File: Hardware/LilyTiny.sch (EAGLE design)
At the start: 14 parts, among them U1 ATTINY85

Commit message: Updating files to more clearly differentiate between Tiny/Twinkle
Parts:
- added LOGO2: SFE_LOGO_FLAME.1_INCH, SparkFun-Aesthetics:SFE_LOGO_FLAME.1_INCH
- added U$1: REVISION, SparkFun-Aesthetics:REVISION
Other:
- note added: "P.Lewis, T.Klopfenstein"
- note added: "V12"
- note removed: "Revised by: Pete Lewis"
- note removed: "V11"
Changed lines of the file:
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@@
 <?xml version="1.0" encoding="utf-8"?>
 <!DOCTYPE eagle SYSTEM "eagle.dtd">
-<eagle version="6.4">
+<eagle version="6.5.0">
 <drawing>
 <settings>
@@
 <grid distance="0.1" unitdist="inch" unit="inch" style="lines" multiple="1" display="no" altdistance="0.01" altunitdist="inch" altunit="inch"/>
 <layers>
-<layer number="1" name="Top" color="4" fill="1" visible="yes" active="no"/>
-<layer number="2" name="Route2" color="1" fill="3" visible="yes" active="no"/>
-<layer number="3" name="Route3" color="4" fill="3" visible="yes" active="no"/>
-<layer number="4" name="Route4" color="1" fill="4" visible="yes" active="no"/>
-<layer number="5" name="Route5" color="4" fill="4" visible="yes" active="no"/>
-<layer number="6" name="Route6" color="1" fill="8" visible="yes" active="no"/>
-<layer number="7" name="Route7" color="4" fill="8" visible="yes" active="no"/>
-<layer number="8" name="Route8" color="1" fill="2" visible="yes" active="no"/>
-<layer number="9" name="Route9" color="4" fill="2" visible="yes" active="no"/>
-<layer number="10" name="Route10" color="1" fill="7" visible="yes" active="no"/>
-<layer number="11" name="Route11" color="4" fill="7" visible="yes" active="no"/>
-<layer number="12" name="Route12" color="1" fill="5" visible="yes" active="no"/>
-<layer number="13" name="Route13" color="4" fill="5" visible="yes" active="no"/>
-<layer number="14" name="Route14" color="1" fill="6" visible="yes" active="no"/>
-<layer number="15" name="Route15" color="4" fill="6" visible="yes" active="no"/>
-<layer number="16" name="Bottom" color="1" fill="1" visible="yes" active="no"/>
-<layer number="17" name="Pads" color="2" fill="1" visible="yes" active="no"/>
-<layer number="18" name="Vias" color="2" fill="1" visible="yes" active="no"/>
-<layer number="19" name="Unrouted" color="6" fill="1" visible="yes" active="no"/>
-<layer number="20" name="Dimension" color="6" fill="1" visible="yes" active="no"/>
-<layer number="21" name="tPlace" color="16" fill="1" visible="yes" active="no"/>
-<layer number="22" name="bPlace" color="14" fill="1" visible="yes" active="no"/>
-<layer number="23" name="tOrigins" color="15" fill="1" visible="yes" active="no"/>
-<layer number="24" name="bOrigins" color="15" fill="1" visible="yes" active="no"/>
-<layer number="25" name="tNames" color="7" fill="1" visible="yes" active="no"/>
-<layer number="26" name="bNames" color="7" fill="1" visible="yes" active="no"/>
-<layer number="27" name="tValues" color="7" fill="1" visible="yes" active="no"/>
-<layer number="28" name="bValues" color="7" fill="1" visible="yes" active="no"/>
+<layer number="1" name="Top" color="4" fill="1" visible="no" active="no"/>
+<layer number="2" name="Route2" color="1" fill="3" visible="no" active="no"/>
+<layer number="3" name="Route3" color="4" fill="3" visible="no" active="no"/>
+<layer number="4" name="Route4" color="1" fill="4" visible="no" active="no"/>
+<layer number="5" name="Route5" color="4" fill="4" visible="no" active="no"/>
+<layer number="6" name="Route6" color="1" fill="8" visible="no" active="no"/>
+<layer number="7" name="Route7" color="4" fill="8" visible="no" active="no"/>
+<layer number="8" name="Route8" color="1" fill="2" visible="no" active="no"/>
+<layer number="9" name="Route9" color="4" fill="2" visible="no" active="no"/>
+<layer number="10" name="Route10" color="1" fill="7" visible="no" active="no"/>
+<layer number="11" name="Route11" color="4" fill="7" visible="no" active="no"/>
+<layer number="12" name="Route12" color="1" fill="5" visible="no" active="no"/>
+<layer number="13" name="Route13" color="4" fill="5" visible="no" active="no"/>
+<layer number="14" name="Route14" color="1" fill="6" visible="no" active="no"/>
+<layer number="15" name="Route15" color="4" fill="6" visible="no" active="no"/>
+<layer number="16" name="Bottom" color="1" fill="1" visible="no" active="no"/>
+<layer number="17" name="Pads" color="2" fill="1" visible="no" active="no"/>
+<layer number="18" name="Vias" color="2" fill="1" visible="no" active="no"/>
+<layer number="19" name="Unrouted" color="6" fill="1" visible="no" active="no"/>
+<layer number="20" name="Dimension" color="6" fill="1" visible="no" active="no"/>
+<layer number="21" name="tPlace" color="16" fill="1" visible="no" active="no"/>
+<layer number="22" name="bPlace" color="14" fill="1" visible="no" active="no"/>
+<layer number="23" name="tOrigins" color="15" fill="1" visible="no" active="no"/>
+<layer number="24" name="bOrigins" color="15" fill="1" visible="no" active="no"/>
+<layer number="25" name="tNames" color="7" fill="1" visible="no" active="no"/>
+<layer number="26" name="bNames" color="7" fill="1" visible="no" active="no"/>
+<layer number="27" name="tValues" color="7" fill="1" visible="no" active="no"/>
+<layer number="28" name="bValues" color="7" fill="1" visible="no" active="no"/>
 <layer number="29" name="tStop" color="7" fill="3" visible="no" active="no"/>
 <layer number="30" name="bStop" color="7" fill="6" visible="no" active="no"/>
@@
 <layer number="35" name="tGlue" color="7" fill="4" visible="no" active="no"/>
 <layer number="36" name="bGlue" color="7" fill="5" visible="no" active="no"/>
-<layer number="37" name="tTest" color="7" fill="1" visible="yes" active="no"/>
-<layer number="38" name="bTest" color="7" fill="1" visible="yes" active="no"/>
+<layer number="37" name="tTest" color="7" fill="1" visible="no" active="no"/>
+<layer number="38" name="bTest" color="7" fill="1" visible="no" active="no"/>
 <layer number="39" name="tKeepout" color="4" fill="11" visible="no" active="no"/>
 <layer number="40" name="bKeepout" color="1" fill="11" visible="no" active="no"/>
@@
 <layer number="44" name="Drills" color="7" fill="1" visible="no" active="no"/>
 <layer number="45" name="Holes" color="7" fill="1" visible="no" active="no"/>
-<layer number="46" name="Milling" color="3" fill="1" visible="yes" active="no"/>
-<layer number="47" name="Measures" color="7" fill="1" visible="yes" active="no"/>
-<layer number="48" name="Document" color="7" fill="1" visible="yes" active="no"/>
-<layer number="49" name="Reference" color="7" fill="1" visible="yes" active="no"/>
-<layer number="50" name="dxf" color="7" fill="1" visible="yes" active="no"/>
-<layer number="51" name="tDocu" color="6" fill="1" visible="yes" active="no"/>
-<layer number="52" name="bDocu" color="7" fill="1" visible="yes" active="no"/>
-<layer number="53" name="tGND_GNDA" color="7" fill="9" visible="yes" active="no"/>
-<layer number="54" name="bGND_GNDA" color="1" fill="9" visible="yes" active="no"/>
-<layer number="56" name="wert" color="7" fill="1" visible="yes" active="no"/>
+<layer number="46" name="Milling" color="3" fill="1" visible="no" active="no"/>
+<layer number="47" name="Measures" color="7" fill="1" visible="no" active="no"/>
+<layer number="48" name="Document" color="7" fill="1" visible="no" active="no"/>
+<layer number="49" name="Reference" color="7" fill="1" visible="no" active="no"/>
+<layer number="50" name="dxf" color="7" fill="1" visible="no" active="no"/>
+<layer number="51" name="tDocu" color="6" fill="1" visible="no" active="no"/>
+<layer number="52" name="bDocu" color="7" fill="1" visible="no" active="no"/>
+<layer number="53" name="tGND_GNDA" color="7" fill="9" visible="no" active="no"/>
+<layer number="54" name="bGND_GNDA" color="1" fill="9" visible="no" active="no"/>
+<layer number="56" name="wert" color="7" fill="1" visible="no" active="no"/>
 <layer number="91" name="Nets" color="2" fill="1" visible="yes" active="yes"/>
 <layer number="92" name="Busses" color="1" fill="1" visible="yes" active="yes"/>
@@
 <part name="FRAME2" library="SparkFun-Aesthetics" deviceset="FRAME-LETTER" device=""/>
 <part name="LOGO1" library="SparkFun-Aesthetics" deviceset="OSHW-LOGO" device="S"/>
+<part name="U$1" library="SparkFun-Aesthetics" deviceset="REVISION" device=""/>
+<part name="LOGO2" library="SparkFun-Aesthetics" deviceset="SFE_LOGO_FLAME" device=".1_INCH"/>
 </parts>
 <sheets>
@@
 <text x="32.766" y="1.27" size="2.1844" layer="91">2</text>
 <text x="32.766" y="-1.27" size="2.1844" layer="91">3</text>
-<text x="66.294" y="-82.296" size="1.778" layer="94">Revised by: Pete Lewis</text>
-<text x="119.38" y="-86.36" size="1.778" layer="94">V11</text>
+<text x="58.674" y="-87.376" size="1.778" layer="94">P.Lewis, T.Klopfenstein</text>
+<text x="119.38" y="-86.36" size="1.778" layer="94">V12</text>
 </plain>
 <instances>
@@
 <instance part="U$7" gate="G$1" x="30.48" y="7.62"/>
 <instance part="P+2" gate="1" x="0" y="-20.32"/>
-<instance part="U$8" gate="G$1" x="111.76" y="-66.04"/>
+<instance part="U$8" gate="G$1" x="116.84" y="-76.2"/>
 <instance part="JP1" gate="G$1" x="127" y="-63.5"/>
 <instance part="JP2" gate="G$1" x="127" y="-68.58"/>
@@
 <instance part="FRAME2" gate="G$2" x="27.94" y="-93.98"/>
 <instance part="LOGO1" gate="G$1" x="116.84" y="-48.26"/>
+<instance part="U$1" gate="G$1" x="29.718" y="-87.122"/>
+<instance part="LOGO2" gate="G$1" x="96.52" y="-58.42"/>
 </instances>
 <busses>

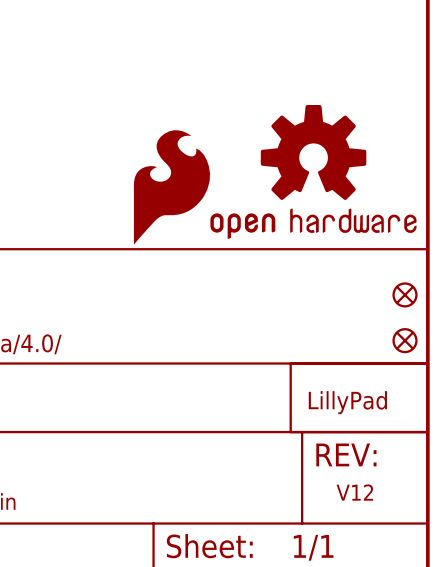
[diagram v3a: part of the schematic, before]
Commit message: Added regular fid to board. Deleted old gerbs
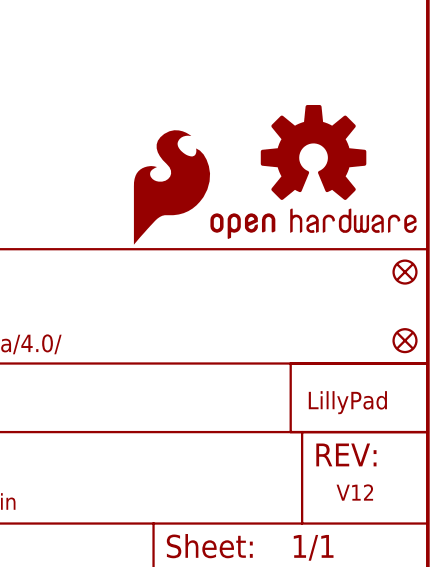
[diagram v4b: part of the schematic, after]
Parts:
- removed JP1, JP2: FIDUCIALUFIDUCIAL, SparkFun:FIDUCIALUFIDUCIAL
- added FID1, FID2: FIDUCIAL1X2, SparkFun-Aesthetics:FIDUCIAL1X2
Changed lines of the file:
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@@
 <part name="P+2" library="SparkFun" deviceset="VCC" device=""/>
 <part name="U$8" library="LilyPad-Wearables" deviceset="LOGO-LP" device="L"/>
-<part name="JP1" library="SparkFun" deviceset="FIDUCIAL" device="UFIDUCIAL"/>
-<part name="JP2" library="SparkFun" deviceset="FIDUCIAL" device="UFIDUCIAL"/>
 <part name="FRAME2" library="SparkFun-Aesthetics" deviceset="FRAME-LETTER" device=""/>
 <part name="LOGO1" library="SparkFun-Aesthetics" deviceset="OSHW-LOGO" device="S"/>
 <part name="U$1" library="SparkFun-Aesthetics" deviceset="REVISION" device=""/>
 <part name="LOGO2" library="SparkFun-Aesthetics" deviceset="SFE_LOGO_FLAME" device=".1_INCH"/>
+<part name="FID1" library="SparkFun-Aesthetics" deviceset="FIDUCIAL" device="1X2"/>
+<part name="FID2" library="SparkFun-Aesthetics" deviceset="FIDUCIAL" device="1X2"/>
 </parts>
 <sheets>
@@
 <instance part="P+2" gate="1" x="0" y="-20.32"/>
 <instance part="U$8" gate="G$1" x="116.84" y="-76.2"/>
-<instance part="JP1" gate="G$1" x="127" y="-63.5"/>
-<instance part="JP2" gate="G$1" x="127" y="-68.58"/>
 <instance part="FRAME2" gate="G$1" x="-119.38" y="-93.98"/>
 <instance part="FRAME2" gate="G$2" x="27.94" y="-93.98"/>
@@
 <instance part="U$1" gate="G$1" x="29.718" y="-87.122"/>
 <instance part="LOGO2" gate="G$1" x="96.52" y="-58.42"/>
+<instance part="FID1" gate="G$1" x="127" y="-60.96"/>
+<instance part="FID2" gate="G$1" x="127" y="-68.58"/>
 </instances>
 <busses>

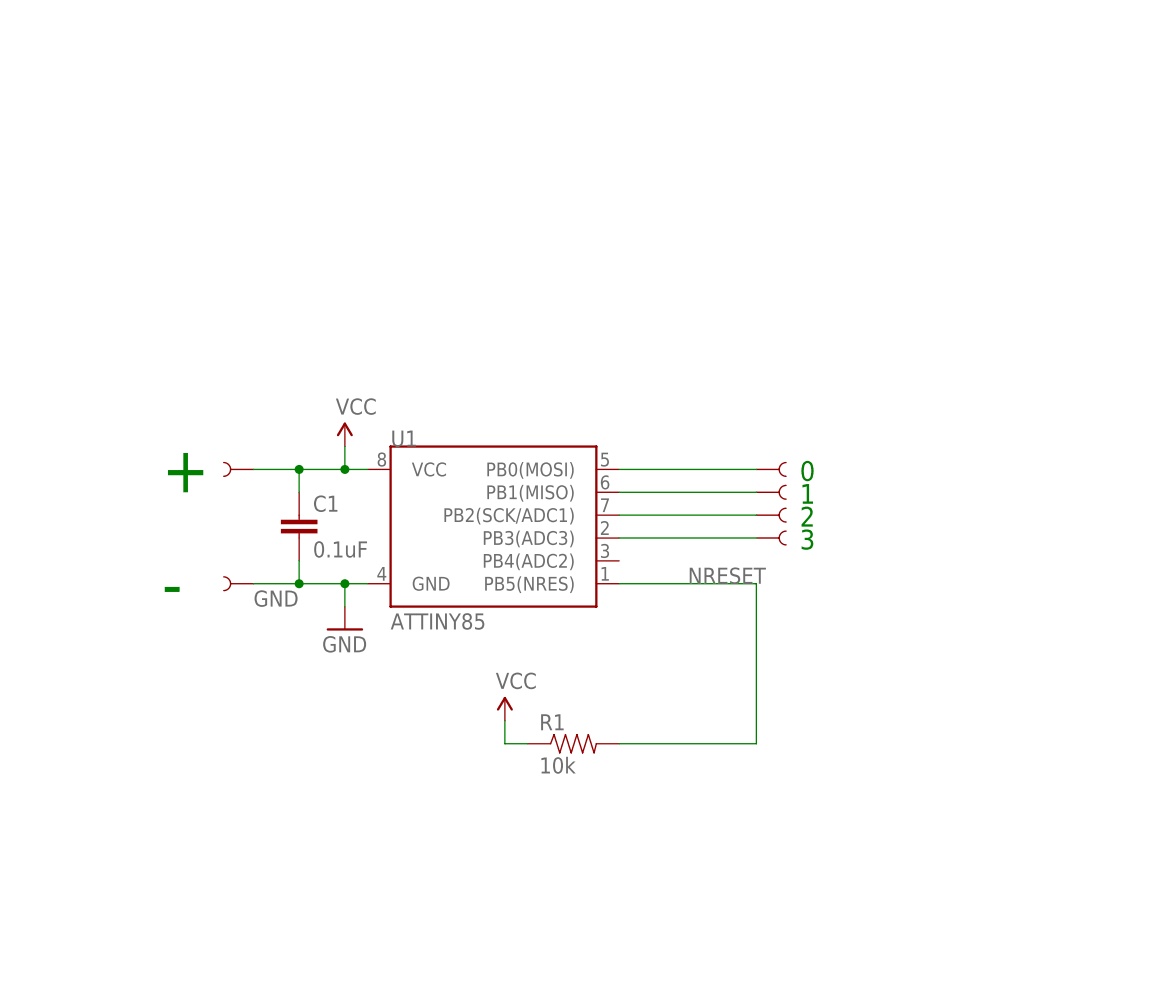
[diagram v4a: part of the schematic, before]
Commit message: Switched programming lines from vias to device
-Used AVR_SPI_PRG_6.dev with the new "TEST_POINTS" package (which
include the necessary stop mask).

-Centered symbols in schematic.
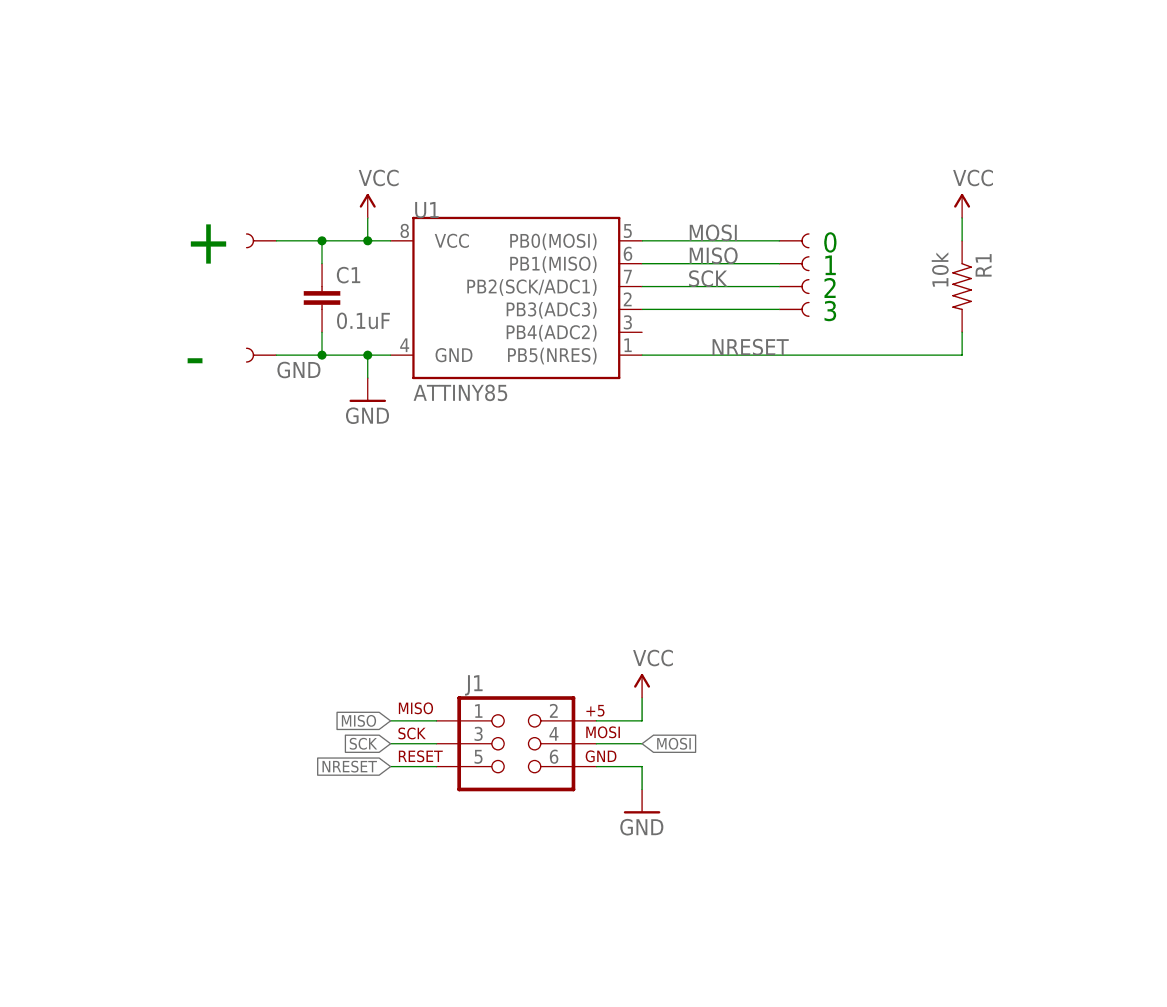
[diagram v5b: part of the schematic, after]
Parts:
- added J1: AVR_SPI_PRG_6TESTPOINTS, SparkFun-Connectors:AVR_SPI_PRG_6TESTPOINTS
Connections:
- removed net N$3: U$7.1, U1.PB0(MOSI)
- removed net N$4: U$3.1, U1.PB1(MISO)
- removed net N$5: U$4.1, U1.PB2(SCK/ADC1)
- new net MISO: J1.1, U$3.1, U1.PB1(MISO)
- new net MOSI: J1.4, U$7.1, U1.PB0(MOSI)
- new net SCK: J1.3, U$4.1, U1.PB2(SCK/ADC1)
- net GND: now also J1.6
- net NRESET: now also J1.5
- net VCC: now also J1.2
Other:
- moved on the sheet: C1, R1, U1
